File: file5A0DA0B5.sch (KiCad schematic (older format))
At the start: 29 parts, among them U14 AK4452, U15 NE5534, U16 NE5534

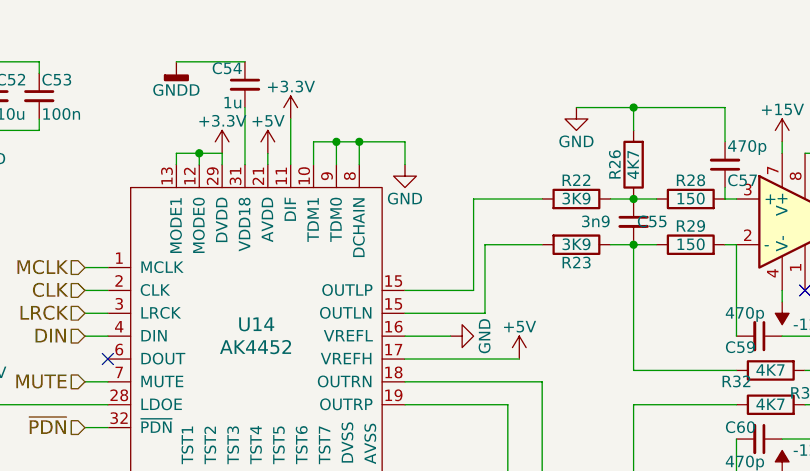
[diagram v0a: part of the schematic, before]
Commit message: Updated schematics and part number fields
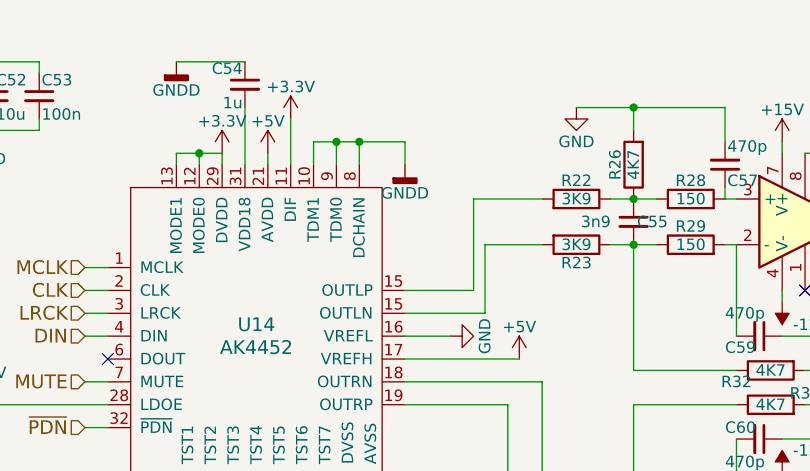
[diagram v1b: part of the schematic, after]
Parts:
- R22: MPN (none) -> RC0805FR-073K9L
- R28: MPN (none) -> RC0805FR-07150RL
- R32: MPN (none) -> RC0805FR-074K7L
- U14: footprint (none) -> Housings_DFN_QFN:QFN-32-1EP_5x5mm_Pitch0.5mm
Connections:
- net GND: no longer U14.10 (TDM1), U14.8 (DCHAIN), U14.9 (TDM0)
- net GNDD: now also U14.10 (TDM1), U14.8 (DCHAIN), U14.9 (TDM0)
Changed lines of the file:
@@
 F 0 "U14" H 5800 3700 60  0000 C CNN
 F 1 "AK4452" H 5800 3600 60  0000 C CNN
-F 2 "" H 5800 3600 60  0001 C CNN
+F 2 "Housings_DFN_QFN:QFN-32-1EP_5x5mm_Pitch0.5mm" H 5800 3600 60  0001 C CNN
 F 3 "" H 5800 3600 60  0001 C CNN
 F 4 "AK4452VN" H 5800 3600 60  0001 C CNN "mpn"
@@
 $EndComp
 $Comp
-L GNDD #PWR044
+L GNDD #PWR54
 U 1 1 5A0DABEF
 P 6200 4350
-F 0 "#PWR044" H 6200 4100 50  0001 C CNN
+F 0 "#PWR54" H 6200 4100 50  0001 C CNN
 F 1 "GNDD" H 6200 4225 50  0000 C CNN
 F 2 "" H 6200 4350 50  0001 C CNN
@@
 $EndComp
 $Comp
-L GND #PWR045
+L GND #PWR51
 U 1 1 5A0DAC06
 P 5800 4350
-F 0 "#PWR045" H 5800 4100 50  0001 C CNN
+F 0 "#PWR51" H 5800 4100 50  0001 C CNN
 F 1 "GND" H 5800 4200 50  0000 C CNN
 F 2 "" H 5800 4350 50  0001 C CNN
@@
 	6200 4350 6200 4250
 $Comp
-L GND #PWR046
+L GND #PWR55
 U 1 1 5A0DAC84
 P 6400 4250
-F 0 "#PWR046" H 6400 4000 50  0001 C CNN
+F 0 "#PWR55" H 6400 4000 50  0001 C CNN
 F 1 "GND" H 6400 4100 50  0000 C CNN
 F 2 "" H 6400 4250 50  0001 C CNN
@@
 	6300 4250 6400 4250
 $Comp
-L GND #PWR047
+L GND #PWR57
 U 1 1 5A0DACAA
 P 6650 3550
-F 0 "#PWR047" H 6650 3300 50  0001 C CNN
+F 0 "#PWR57" H 6650 3300 50  0001 C CNN
 F 1 "GND" H 6650 3400 50  0000 C CNN
 F 2 "" H 6650 3550 50  0001 C CNN
@@
 	6450 3550 6650 3550
 $Comp
-L +5V #PWR048
+L +5V #PWR58
 U 1 1 5A0DACCB
 P 6950 3650
-F 0 "#PWR048" H 6950 3500 50  0001 C CNN
+F 0 "#PWR58" H 6950 3500 50  0001 C CNN
 F 1 "+5V" H 6950 3790 50  0000 C CNN
 F 2 "" H 6950 3650 50  0001 C CNN
@@
 	5050 3250 5150 3250
 $Comp
-L +5V #PWR049
+L +5V #PWR52
 U 1 1 5A0DADE7
 P 5850 2750
-F 0 "#PWR049" H 5850 2600 50  0001 C CNN
+F 0 "#PWR52" H 5850 2600 50  0001 C CNN
 F 1 "+5V" H 5850 2890 50  0000 C CNN
 F 2 "" H 5850 2750 50  0001 C CNN
@@
 	5850 2750 5850 2800
 $Comp
-L +3.3V #PWR050
+L +3.3V #PWR50
 U 1 1 5A0DAE0F
 P 5650 2750
-F 0 "#PWR050" H 5650 2600 50  0001 C CNN
+F 0 "#PWR50" H 5650 2600 50  0001 C CNN
 F 1 "+3.3V" H 5650 2890 50  0000 C CNN
 F 2 "" H 5650 2750 50  0001 C CNN
@@
 Connection ~ 5550 2750
 $Comp
-L +3.3V #PWR051
+L +3.3V #PWR53
 U 1 1 5A0DAE74
 P 5950 2600
-F 0 "#PWR051" H 5950 2450 50  0001 C CNN
+F 0 "#PWR53" H 5950 2450 50  0001 C CNN
 F 1 "+3.3V" H 5950 2740 50  0000 C CNN
 F 2 "" H 5950 2600 50  0001 C CNN
@@
 Wire Wire Line
 	5950 2600 5950 2800
-$Comp
-L GND #PWR052
-U 1 1 5A0DAEA2
-P 6450 2800
-F 0 "#PWR052" H 6450 2550 50  0001 C CNN
-F 1 "GND" H 6450 2650 50  0000 C CNN
-F 2 "" H 6450 2800 50  0001 C CNN
-F 3 "" H 6450 2800 50  0001 C CNN
-	1    6450 2800
-	1    0    0    -1
-$EndComp
 Wire Wire Line
 	6050 2800 6050 2700
@@
 Connection ~ 6150 2700
 $Comp
-L +3.3V #PWR053
+L +3.3V #PWR48
 U 1 1 5A0DAEF7
 P 4600 3850
-F 0 "#PWR053" H 4600 3700 50  0001 C CNN
+F 0 "#PWR48" H 4600 3700 50  0001 C CNN
 F 1 "+3.3V" H 4600 3990 50  0000 C CNN
 F 2 "" H 4600 3850 50  0001 C CNN
@@
 $EndComp
 $Comp
-L GND #PWR054
+L GND #PWR45
 U 1 1 5A0DB5F4
 P 4100 2650
-F 0 "#PWR054" H 4100 2400 50  0001 C CNN
+F 0 "#PWR45" H 4100 2400 50  0001 C CNN
 F 1 "GND" H 4100 2500 50  0000 C CNN
 F 2 "" H 4100 2650 50  0001 C CNN
@@
 $EndComp
 $Comp
-L +3.3V #PWR055
+L +3.3V #PWR44
 U 1 1 5A0DB613
 P 4100 2350
-F 0 "#PWR055" H 4100 2200 50  0001 C CNN
+F 0 "#PWR44" H 4100 2200 50  0001 C CNN
 F 1 "+3.3V" H 4100 2490 50  0000 C CNN
 F 2 "" H 4100 2350 50  0001 C CNN
@@
 Connection ~ 4600 2650
 $Comp
-L +5V #PWR056
+L +5V #PWR46
 U 1 1 5A0DB78F
 P 4600 2350
-F 0 "#PWR056" H 4600 2200 50  0001 C CNN
+F 0 "#PWR46" H 4600 2200 50  0001 C CNN
 F 1 "+5V" H 4600 2490 50  0000 C CNN
 F 2 "" H 4600 2350 50  0001 C CNN
@@
 $EndComp
 $Comp
-L GNDD #PWR057
+L GNDD #PWR47
 U 1 1 5A0DB7BD
 P 4600 2650
-F 0 "#PWR057" H 4600 2400 50  0001 C CNN
+F 0 "#PWR47" H 4600 2400 50  0001 C CNN
 F 1 "GNDD" H 4600 2525 50  0000 C CNN
 F 2 "" H 4600 2650 50  0001 C CNN
@@
 $EndComp
 $Comp
-L GNDD #PWR058
+L GNDD #PWR49
 U 1 1 5A0DB7EC
 P 5450 2350
-F 0 "#PWR058" H 5450 2100 50  0001 C CNN
+F 0 "#PWR49" H 5450 2100 50  0001 C CNN
 F 1 "GNDD" H 5450 2225 50  0000 C CNN
 F 2 "" H 5450 2350 50  0001 C CNN
@@
 F 2 "Resistors_SMD:R_0805_HandSoldering" V 7130 2950 50  0001 C CNN
 F 3 "" H 7200 2950 50  0001 C CNN
+F 4 "RC0805FR-073K9L" V 7200 2950 60  0001 C CNN "MPN"
 	1    7200 2950
 	0    1    -1   0
@@
 F 2 "Resistors_SMD:R_0805_HandSoldering" V 7980 3700 50  0001 C CNN
 F 3 "" H 8050 3700 50  0001 C CNN
+F 4 "RC0805FR-074K7L" V 8050 3700 60  0001 C CNN "MPN"
 	1    8050 3700
 	0    -1   1    0
@@
 F 2 "Resistors_SMD:R_0805_HandSoldering" V 7630 2950 50  0001 C CNN
 F 3 "" H 7700 2950 50  0001 C CNN
+F 4 "RC0805FR-07150RL" V 7700 2950 60  0001 C CNN "MPN"
 	1    7700 2950
 	0    -1   -1   0
@@
 	7850 2900 7850 2950
 $Comp
-L GND #PWR059
+L GND #PWR59
 U 1 1 5A0DD156
 P 7200 2550
-F 0 "#PWR059" H 7200 2300 50  0001 C CNN
+F 0 "#PWR59" H 7200 2300 50  0001 C CNN
 F 1 "GND" H 7200 2400 50  0000 C CNN
 F 2 "" H 7200 2550 50  0001 C CNN
@@
 Connection ~ 7450 2550
 $Comp
-L +15V #PWR060
+L +15V #PWR61
 U 1 1 5A0DD2FF
 P 8100 2700
-F 0 "#PWR060" H 8100 2550 50  0001 C CNN
+F 0 "#PWR61" H 8100 2550 50  0001 C CNN
 F 1 "+15V" H 8100 2840 50  0000 C CNN
 F 2 "" H 8100 2700 50  0001 C CNN
@@
 	8100 2750 8100 2700
 $Comp
-L -12VA #PWR061
+L -12VA #PWR62
 U 1 1 5A0DD3DC
 P 8100 3400
-F 0 "#PWR061" H 8100 3250 50  0001 C CNN
+F 0 "#PWR62" H 8100 3250 50  0001 C CNN
 F 1 "-12VA" H 7950 3500 50  0000 C CNN
 F 2 "" H 8100 3400 50  0001 C CNN
@@
 	7850 4650 7850 4600
 $Comp
-L GND #PWR062
+L GND #PWR60
 U 1 1 5A0DDFBD
 P 7200 5000
-F 0 "#PWR062" H 7200 4750 50  0001 C CNN
+F 0 "#PWR60" H 7200 4750 50  0001 C CNN
 F 1 "GND" H 7200 4850 50  0000 C CNN
 F 2 "" H 7200 5000 50  0001 C CNN
@@
 Connection ~ 7450 5000
 $Comp
-L +15V #PWR063
+L +15V #PWR64
 U 1 1 5A0DDFC7
 P 8100 4850
-F 0 "#PWR063" H 8100 4700 50  0001 C CNN
+F 0 "#PWR64" H 8100 4700 50  0001 C CNN
 F 1 "+15V" H 8100 4990 50  0000 C CNN
 F 2 "" H 8100 4850 50  0001 C CNN
@@
 	8100 4800 8100 4850
 $Comp
-L -12VA #PWR064
+L -12VA #PWR63
 U 1 1 5A0DDFCE
 P 8100 4150
-F 0 "#PWR064" H 8100 4000 50  0001 C CNN
+F 0 "#PWR63" H 8100 4000 50  0001 C CNN
 F 1 "-12VA" H 7950 4250 50  0000 C CNN
 F 2 "" H 8100 4150 50  0001 C CNN
@@
 	1    0    0    -1
 $EndComp
+$Comp
+L GNDD #PWR56
+U 1 1 5A28319F
+P 6450 2800
+F 0 "#PWR56" H 6450 2550 50  0001 C CNN
+F 1 "GNDD" H 6450 2675 50  0000 C CNN
+F 2 "" H 6450 2800 50  0001 C CNN
+F 3 "" H 6450 2800 50  0001 C CNN
+	1    6450 2800
+	1    0    0    -1
+$EndComp

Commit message: Began PCB layout
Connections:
- net +3V3 renamed +3.3VA
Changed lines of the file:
@@
 $EndComp
 $Comp
-L GNDD #PWR54
+L GNDD #PWR020
 U 1 1 5A0DABEF
 P 6200 4350
-F 0 "#PWR54" H 6200 4100 50  0001 C CNN
+F 0 "#PWR020" H 6200 4100 50  0001 C CNN
 F 1 "GNDD" H 6200 4225 50  0000 C CNN
 F 2 "" H 6200 4350 50  0001 C CNN
@@
 $EndComp
 $Comp
-L GND #PWR51
+L GND #PWR021
 U 1 1 5A0DAC06
 P 5800 4350
-F 0 "#PWR51" H 5800 4100 50  0001 C CNN
+F 0 "#PWR021" H 5800 4100 50  0001 C CNN
 F 1 "GND" H 5800 4200 50  0000 C CNN
 F 2 "" H 5800 4350 50  0001 C CNN
@@
 	6200 4350 6200 4250
 $Comp
-L GND #PWR55
+L GND #PWR022
 U 1 1 5A0DAC84
 P 6400 4250
-F 0 "#PWR55" H 6400 4000 50  0001 C CNN
+F 0 "#PWR022" H 6400 4000 50  0001 C CNN
 F 1 "GND" H 6400 4100 50  0000 C CNN
 F 2 "" H 6400 4250 50  0001 C CNN
@@
 	6300 4250 6400 4250
 $Comp
-L GND #PWR57
+L GND #PWR023
 U 1 1 5A0DACAA
 P 6650 3550
-F 0 "#PWR57" H 6650 3300 50  0001 C CNN
+F 0 "#PWR023" H 6650 3300 50  0001 C CNN
 F 1 "GND" H 6650 3400 50  0000 C CNN
 F 2 "" H 6650 3550 50  0001 C CNN
@@
 	6450 3550 6650 3550
 $Comp
-L +5V #PWR58
+L +5V #PWR024
 U 1 1 5A0DACCB
 P 6950 3650
-F 0 "#PWR58" H 6950 3500 50  0001 C CNN
+F 0 "#PWR024" H 6950 3500 50  0001 C CNN
 F 1 "+5V" H 6950 3790 50  0000 C CNN
 F 2 "" H 6950 3650 50  0001 C CNN
@@
 	5050 3250 5150 3250
 $Comp
-L +5V #PWR52
+L +5V #PWR025
 U 1 1 5A0DADE7
 P 5850 2750
-F 0 "#PWR52" H 5850 2600 50  0001 C CNN
+F 0 "#PWR025" H 5850 2600 50  0001 C CNN
 F 1 "+5V" H 5850 2890 50  0000 C CNN
 F 2 "" H 5850 2750 50  0001 C CNN
@@
 Wire Wire Line
 	5850 2750 5850 2800
-$Comp
-L +3.3V #PWR50
-U 1 1 5A0DAE0F
-P 5650 2750
-F 0 "#PWR50" H 5650 2600 50  0001 C CNN
-F 1 "+3.3V" H 5650 2890 50  0000 C CNN
-F 2 "" H 5650 2750 50  0001 C CNN
-F 3 "" H 5650 2750 50  0001 C CNN
-	1    5650 2750
-	1    0    0    -1
-$EndComp
 Wire Wire Line
 	5650 2750 5650 2800
 Wire Wire Line
-	5550 2800 5550 2750
+	5550 2700 5550 2800
 Wire Wire Line
 	5450 2750 5650 2750
@@
 	5450 2800 5450 2750
 Connection ~ 5550 2750
-$Comp
-L +3.3V #PWR53
-U 1 1 5A0DAE74
-P 5950 2600
-F 0 "#PWR53" H 5950 2450 50  0001 C CNN
-F 1 "+3.3V" H 5950 2740 50  0000 C CNN
-F 2 "" H 5950 2600 50  0001 C CNN
-F 3 "" H 5950 2600 50  0001 C CNN
-	1    5950 2600
-	1    0    0    -1
-$EndComp
 Wire Wire Line
 	5950 2600 5950 2800
@@
 	6150 2800 6150 2700
 Connection ~ 6150 2700
-$Comp
-L +3.3V #PWR48
-U 1 1 5A0DAEF7
-P 4600 3850
-F 0 "#PWR48" H 4600 3700 50  0001 C CNN
-F 1 "+3.3V" H 4600 3990 50  0000 C CNN
-F 2 "" H 4600 3850 50  0001 C CNN
-F 3 "" H 4600 3850 50  0001 C CNN
-	1    4600 3850
-	1    0    0    -1
-$EndComp
 Wire Wire Line
 	4600 3850 5150 3850
@@
 $EndComp
 $Comp
-L GND #PWR45
+L GND #PWR026
 U 1 1 5A0DB5F4
 P 4100 2650
-F 0 "#PWR45" H 4100 2400 50  0001 C CNN
+F 0 "#PWR026" H 4100 2400 50  0001 C CNN
 F 1 "GND" H 4100 2500 50  0000 C CNN
 F 2 "" H 4100 2650 50  0001 C CNN
 F 3 "" H 4100 2650 50  0001 C CNN
 	1    4100 2650
-	1    0    0    -1
-$EndComp
-$Comp
-L +3.3V #PWR44
-U 1 1 5A0DB613
-P 4100 2350
-F 0 "#PWR44" H 4100 2200 50  0001 C CNN
-F 1 "+3.3V" H 4100 2490 50  0000 C CNN
-F 2 "" H 4100 2350 50  0001 C CNN
-F 3 "" H 4100 2350 50  0001 C CNN
-	1    4100 2350
 	1    0    0    -1
 $EndComp
@@
 Connection ~ 4600 2650
 $Comp
-L +5V #PWR46
+L +5V #PWR027
 U 1 1 5A0DB78F
 P 4600 2350
-F 0 "#PWR46" H 4600 2200 50  0001 C CNN
+F 0 "#PWR027" H 4600 2200 50  0001 C CNN
 F 1 "+5V" H 4600 2490 50  0000 C CNN
 F 2 "" H 4600 2350 50  0001 C CNN
@@
 $EndComp
 $Comp
-L GNDD #PWR47
+L GNDD #PWR028
 U 1 1 5A0DB7BD
 P 4600 2650
-F 0 "#PWR47" H 4600 2400 50  0001 C CNN
+F 0 "#PWR028" H 4600 2400 50  0001 C CNN
 F 1 "GNDD" H 4600 2525 50  0000 C CNN
 F 2 "" H 4600 2650 50  0001 C CNN
@@
 $EndComp
 $Comp
-L GNDD #PWR49
+L GNDD #PWR029
 U 1 1 5A0DB7EC
 P 5450 2350
-F 0 "#PWR49" H 5450 2100 50  0001 C CNN
+F 0 "#PWR029" H 5450 2100 50  0001 C CNN
 F 1 "GNDD" H 5450 2225 50  0000 C CNN
 F 2 "" H 5450 2350 50  0001 C CNN
@@
 	7850 2900 7850 2950
 $Comp
-L GND #PWR59
+L GND #PWR030
 U 1 1 5A0DD156
 P 7200 2550
-F 0 "#PWR59" H 7200 2300 50  0001 C CNN
+F 0 "#PWR030" H 7200 2300 50  0001 C CNN
 F 1 "GND" H 7200 2400 50  0000 C CNN
 F 2 "" H 7200 2550 50  0001 C CNN
@@
 Connection ~ 7450 2550
 $Comp
-L +15V #PWR61
+L +15V #PWR031
 U 1 1 5A0DD2FF
 P 8100 2700
-F 0 "#PWR61" H 8100 2550 50  0001 C CNN
+F 0 "#PWR031" H 8100 2550 50  0001 C CNN
 F 1 "+15V" H 8100 2840 50  0000 C CNN
 F 2 "" H 8100 2700 50  0001 C CNN
@@
 	8100 2750 8100 2700
 $Comp
-L -12VA #PWR62
+L -12VA #PWR032
 U 1 1 5A0DD3DC
 P 8100 3400
-F 0 "#PWR62" H 8100 3250 50  0001 C CNN
+F 0 "#PWR032" H 8100 3250 50  0001 C CNN
 F 1 "-12VA" H 7950 3500 50  0000 C CNN
 F 2 "" H 8100 3400 50  0001 C CNN
@@
 	7850 4650 7850 4600
 $Comp
-L GND #PWR60
+L GND #PWR033
 U 1 1 5A0DDFBD
 P 7200 5000
-F 0 "#PWR60" H 7200 4750 50  0001 C CNN
+F 0 "#PWR033" H 7200 4750 50  0001 C CNN
 F 1 "GND" H 7200 4850 50  0000 C CNN
 F 2 "" H 7200 5000 50  0001 C CNN
@@
 Connection ~ 7450 5000
 $Comp
-L +15V #PWR64
+L +15V #PWR034
 U 1 1 5A0DDFC7
 P 8100 4850
-F 0 "#PWR64" H 8100 4700 50  0001 C CNN
+F 0 "#PWR034" H 8100 4700 50  0001 C CNN
 F 1 "+15V" H 8100 4990 50  0000 C CNN
 F 2 "" H 8100 4850 50  0001 C CNN
@@
 	8100 4800 8100 4850
 $Comp
-L -12VA #PWR63
+L -12VA #PWR035
 U 1 1 5A0DDFCE
 P 8100 4150
-F 0 "#PWR63" H 8100 4000 50  0001 C CNN
+F 0 "#PWR035" H 8100 4000 50  0001 C CNN
 F 1 "-12VA" H 7950 4250 50  0000 C CNN
 F 2 "" H 8100 4150 50  0001 C CNN
@@
 $EndComp
 $Comp
-L GNDD #PWR56
+L GNDD #PWR036
 U 1 1 5A28319F
 P 6450 2800
-F 0 "#PWR56" H 6450 2550 50  0001 C CNN
+F 0 "#PWR036" H 6450 2550 50  0001 C CNN
 F 1 "GNDD" H 6450 2675 50  0000 C CNN
 F 2 "" H 6450 2800 50  0001 C CNN
@@
 	1    0    0    -1
 $EndComp
+$Comp
+L +3.3VA #PWR037
+U 1 1 5A665224
+P 4600 3800
+F 0 "#PWR037" H 4600 3650 50  0001 C CNN
+F 1 "+3.3VA" H 4600 3940 50  0000 C CNN
+F 2 "" H 4600 3800 50  0001 C CNN
+F 3 "" H 4600 3800 50  0001 C CNN
+	1    4600 3800
+	1    0    0    -1
+$EndComp
+Wire Wire Line
+	4600 3800 4600 3850
+$Comp
+L +3.3VA #PWR038
+U 1 1 5A66541A
+P 4100 2350
+F 0 "#PWR038" H 4100 2200 50  0001 C CNN
+F 1 "+3.3VA" H 4100 2490 50  0000 C CNN
+F 2 "" H 4100 2350 50  0001 C CNN
+F 3 "" H 4100 2350 50  0001 C CNN
+	1    4100 2350
+	1    0    0    -1
+$EndComp
+$Comp
+L +3.3VA #PWR039
+U 1 1 5A665553
+P 5550 2700
+F 0 "#PWR039" H 5550 2550 50  0001 C CNN
+F 1 "+3.3VA" H 5550 2840 50  0000 C CNN
+F 2 "" H 5550 2700 50  0001 C CNN
+F 3 "" H 5550 2700 50  0001 C CNN
+	1    5550 2700
+	1    0    0    -1
+$EndComp
+$Comp
+L +3.3VA #PWR040
+U 1 1 5A665650
+P 5950 2600
+F 0 "#PWR040" H 5950 2450 50  0001 C CNN
+F 1 "+3.3VA" H 5950 2740 50  0000 C CNN
+F 2 "" H 5950 2600 50  0001 C CNN
+F 3 "" H 5950 2600 50  0001 C CNN
+	1    5950 2600
+	1    0    0    -1
+$EndComp

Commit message: updated to new kicad format
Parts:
- C49, C50, C51, C52, C53, C54, C55, C56, C57, C58, C59, C60, C61, C62: symbol C_Small -> Device:C_Small
- R22, R23, R24, R25, R26, R27, R28, R29, R30, R31, R32, R33: symbol R -> Device:R
- U14: symbol AK4452 -> dacparts:AK4452
- U15, U16: symbol NE5534 -> Timer:NE5534

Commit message: started routing PCB
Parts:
- C49, C51, C53, C55, C56, C57, C58, C59, C60, C61, C62: footprint Capacitors_SMD:C_0805_HandSoldering -> Capacitors_SMD:C_0402
- C50, C54: footprint Capacitors_SMD:C_0805_HandSoldering -> Capacitors_SMD:C_0805
- C52: footprint Capacitors_SMD:C_0805_HandSoldering -> Capacitors_SMD:C_1206
- R22, R23, R24, R25, R26, R27, R28, R29, R30, R31, R32, R33: footprint Resistors_SMD:R_0805_HandSoldering -> Resistors_SMD:R_0402
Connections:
- net GNDD is gone; now on net GND: C51.2, C52.2, C53.2, C54.1, U14.10 (TDM1), U14.30 (DVSS), U14.8 (DCHAIN), U14.9 (TDM0)
- net +15V renamed +12V
- net -12VA renamed -12V
